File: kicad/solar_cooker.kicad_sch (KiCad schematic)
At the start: 10 parts, among them SW1 SW_DPST_x2, U1 ATmega2560-16A, U2 microSD, U3 clock_module, U4 e-Paper, U5 anemometer, U6 BME680, U7 PT100

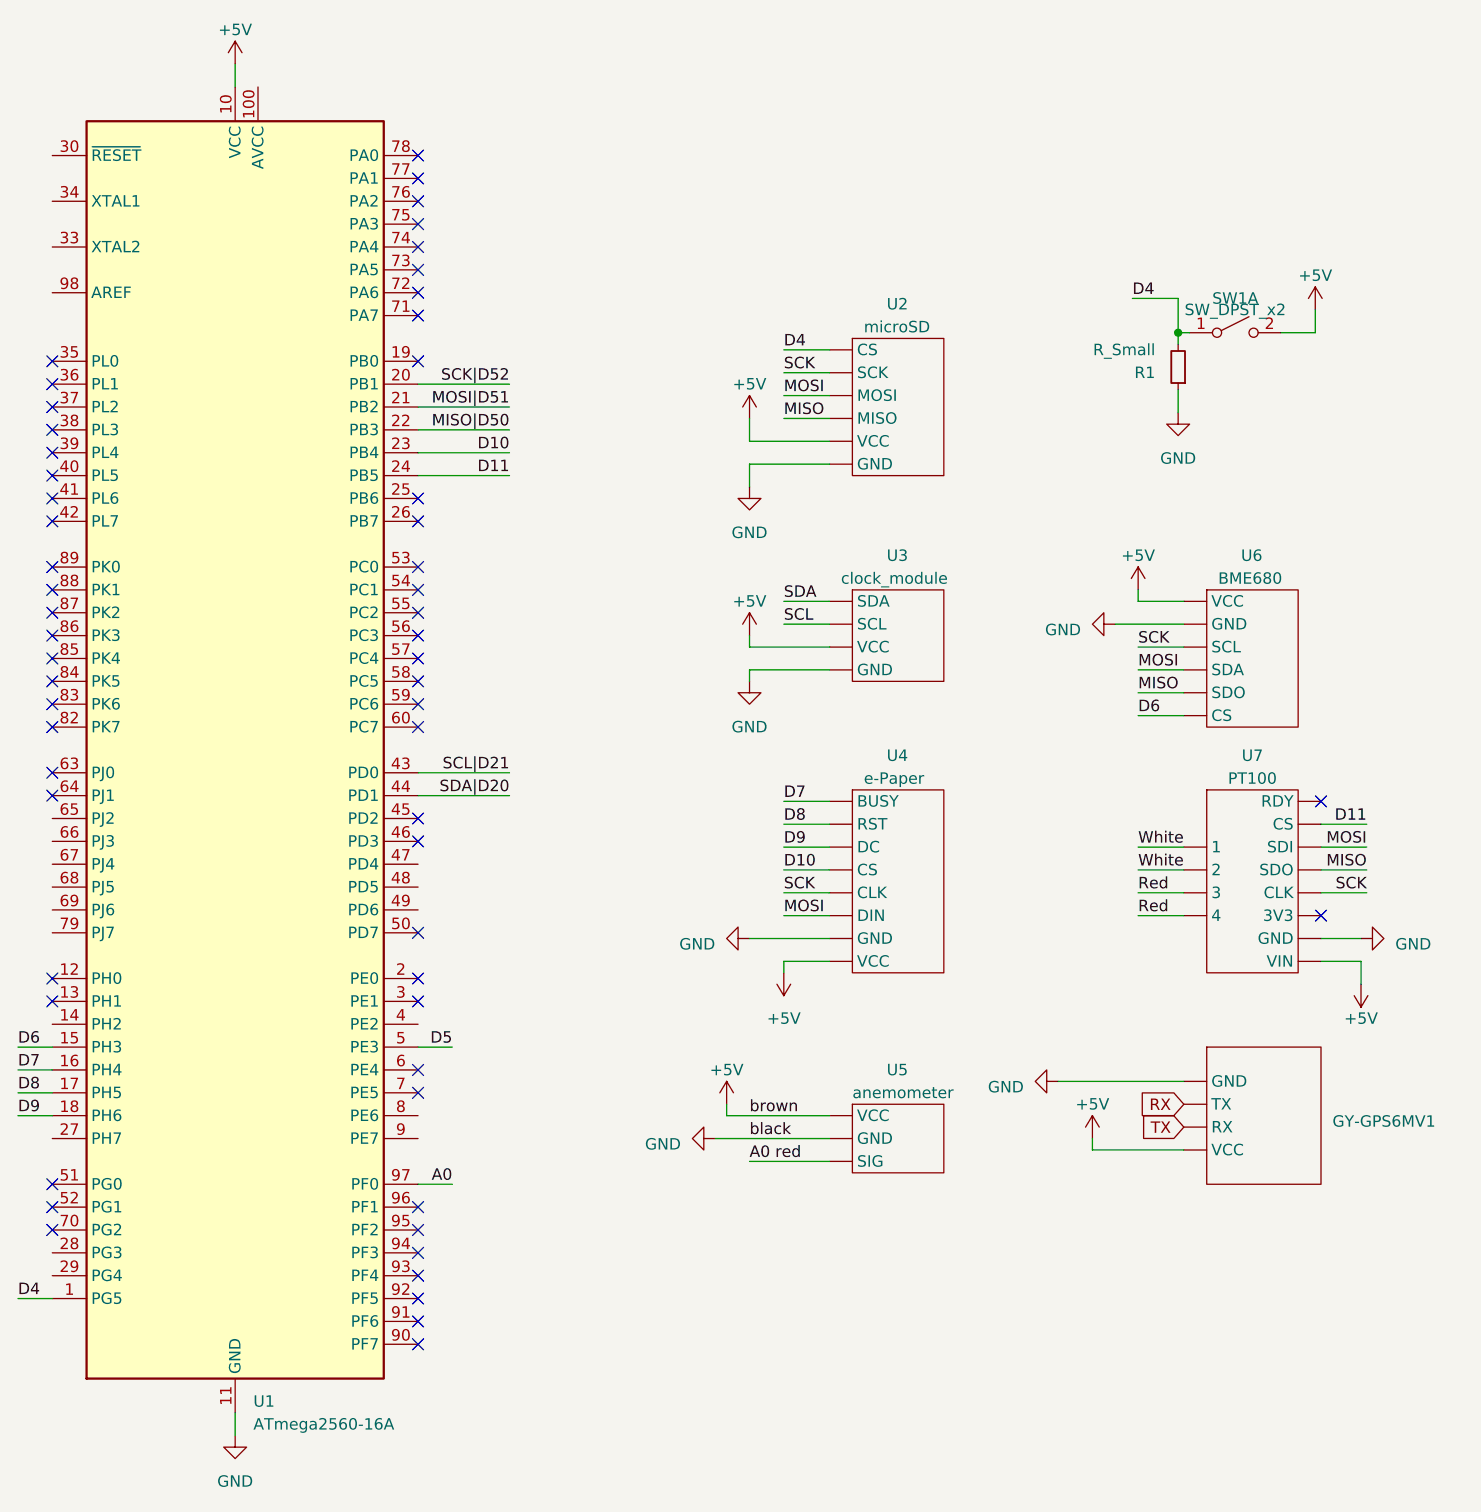
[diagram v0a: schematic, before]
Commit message: GPS schematic update
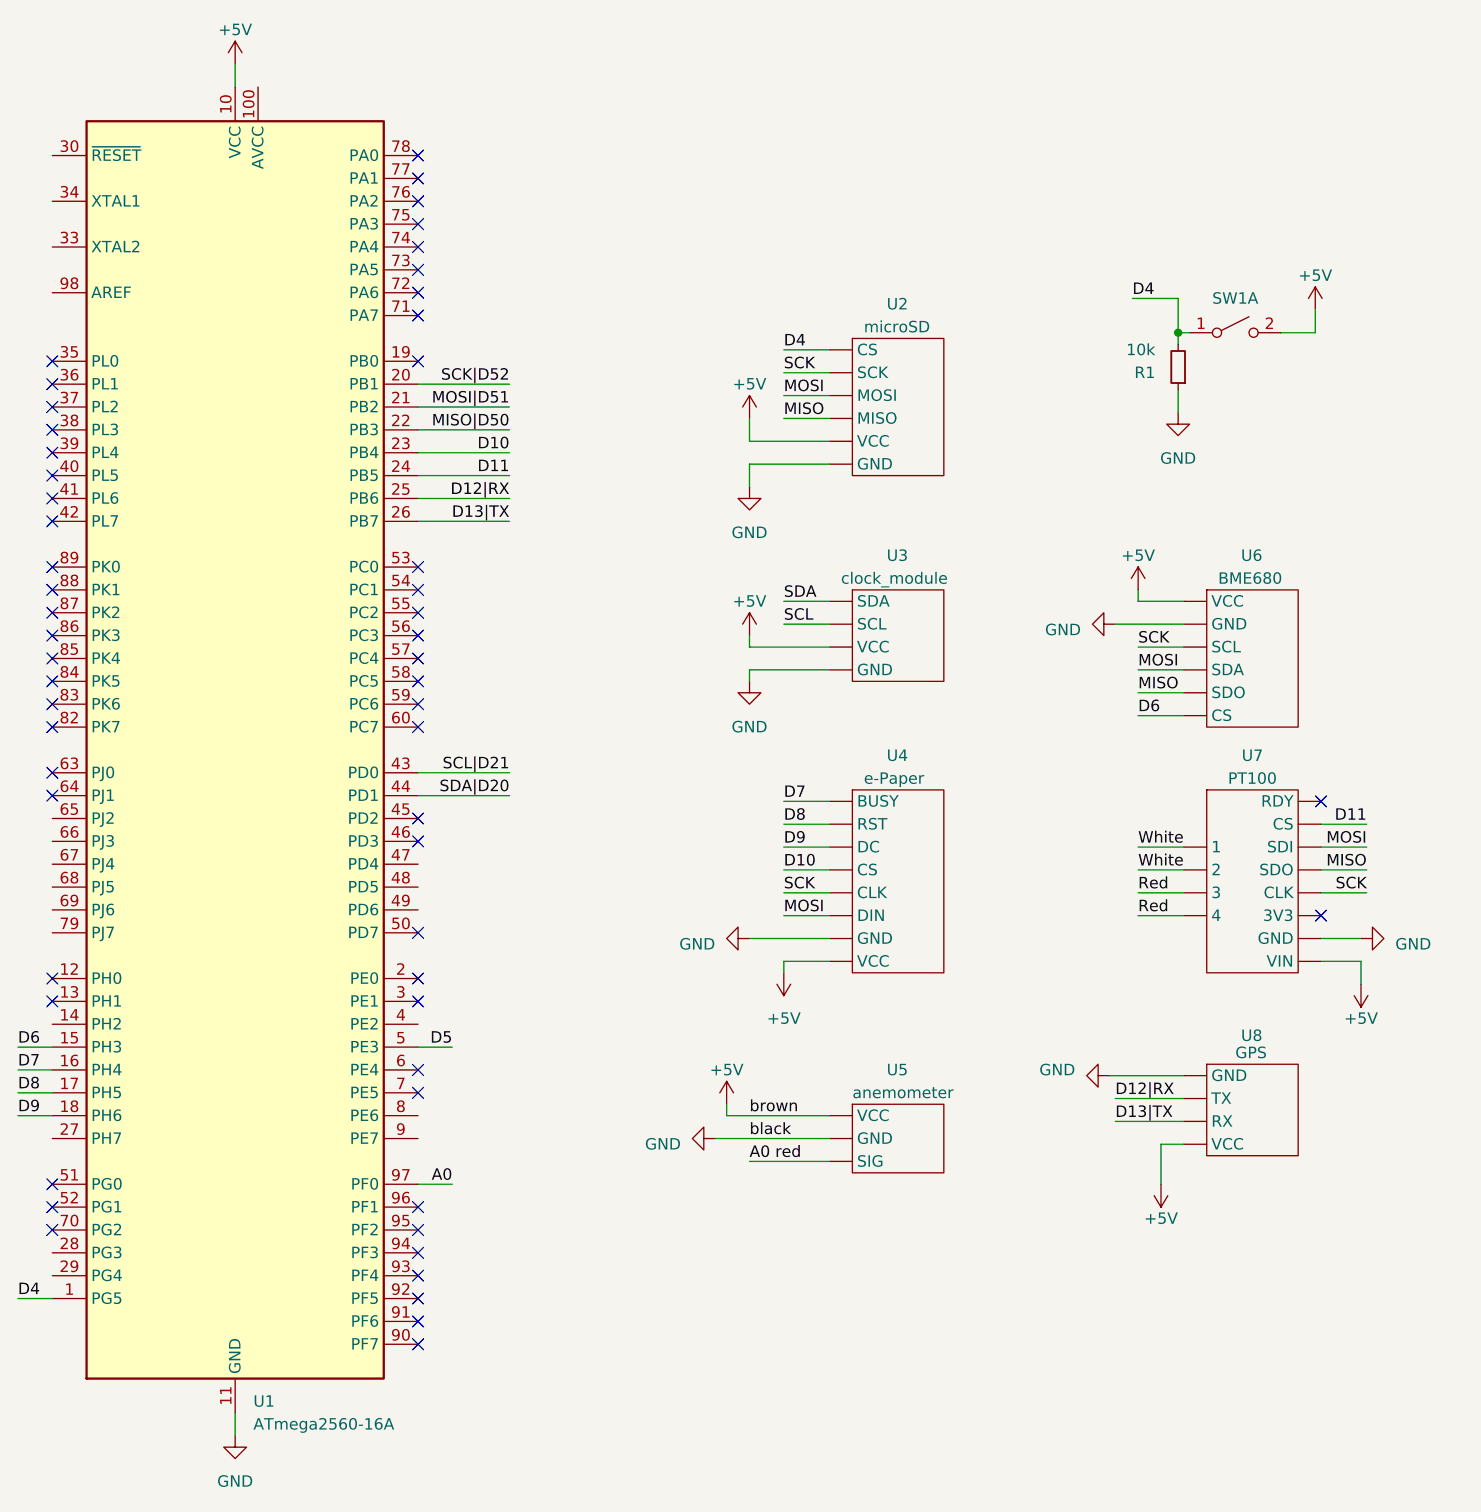
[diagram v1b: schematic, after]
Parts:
- removed GY-GPS6MV1: ~, symbol GPS:GY-GPS6MV2
- added U8: GPS, symbol custom_components:GPS
- R1: value R_Small -> 10k
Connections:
- net +5V: now also U8.4 (VCC)
- net GND: now also U8.1 (GND)
- net D12|RX: now reaches U1.25 (PB6)
- net D12|RX: now also U8.2 (TX)
- net D13|TX: now reaches U1.26 (PB7)
- net D13|TX: now also U8.3 (RX)
- no-connect marks 58 -> 56
